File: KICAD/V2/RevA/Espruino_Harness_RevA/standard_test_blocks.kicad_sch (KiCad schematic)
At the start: 91 parts, among them J201 EXTERNAL_ANALOG_STIMULUS_0_TO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, J301 GROVE_I2C, J302 MCP23017_GPIO, J401 MCP3008_ANALOGUE_BREAKOUT, J402 PIHUT_MICROSD_BREAKOUT_106696, J501 DS18B20_SENSOR_A, J502 DS18B20_SENSOR_B, J503 2K2_DQ_4K7, J504 DS2413_MODULE, J701 UART_PEER_DIAGNOSTIC, J902 PIXEL_SHIFTER_6066, Q301 2N7002, Q302 2N7002, U301 MCP23017-E/SO, U401 MCP3008, U701 TMUX1511

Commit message: Implement RC01 routing baseline metadata
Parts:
- C301, C401, C402, C701, C901: AISLER_MPN (none) -> 100nF 10% 16V X7R 0603
- R308, R311, R705, R706, R707, R708: AISLER_MPN (none) -> 100k 0603 1% 0.1W
- TP101, TP102, TP103, TP104, TP201, TP202, TP203, TP204, TP205, TP301, TP302, TP303, TP304, TP305, TP306, TP401, TP402, TP501, TP502, TP503, TP504, TP505, TP901, TP902: MPN (none) -> 61300111121; now not fitted
- U701: MPN (none) -> TMUX1511PWR

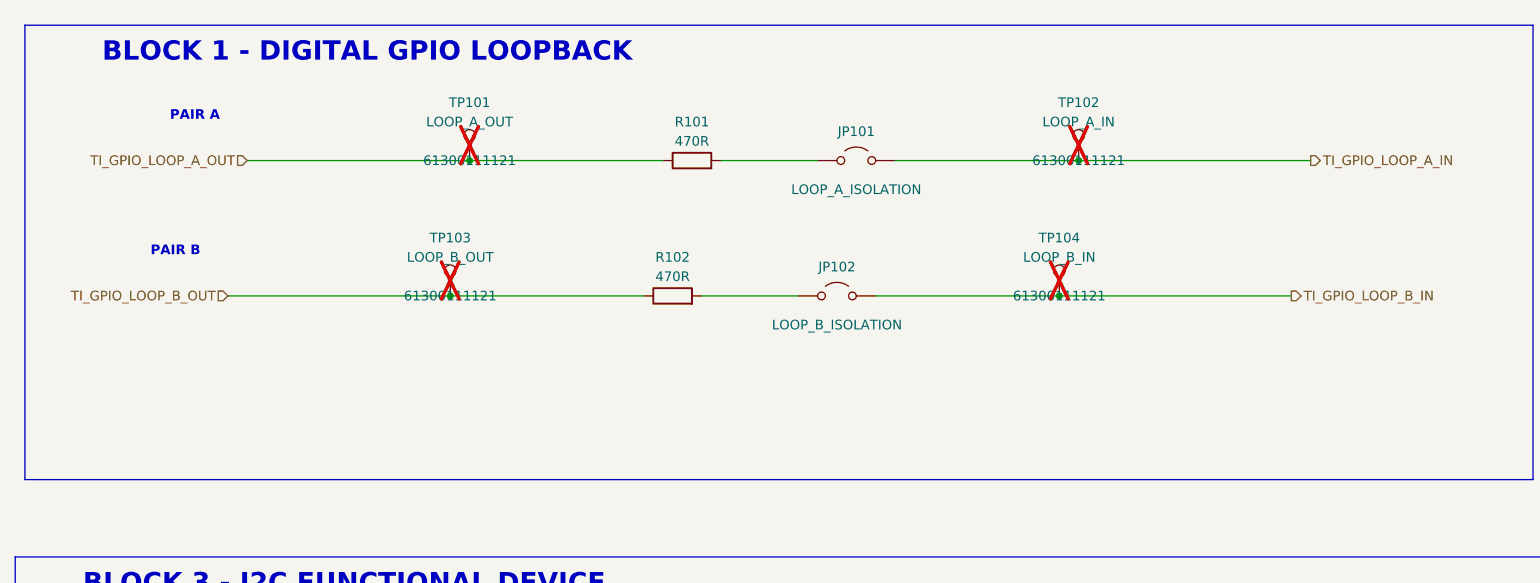
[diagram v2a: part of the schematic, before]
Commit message: Verify TB01 digital GPIO loopback baseline
Accept the two independent 470 ohm protected loopback paths using retained V1 functional evidence and Rev-A SMD component/package review.

Add the project-local isolation-header symbol, exact resistor/header/shunt metadata, focused visual evidence, deterministic TB01 contract, clean hierarchy ERC, synchronized PCB metadata and recorded downstream layout checks.
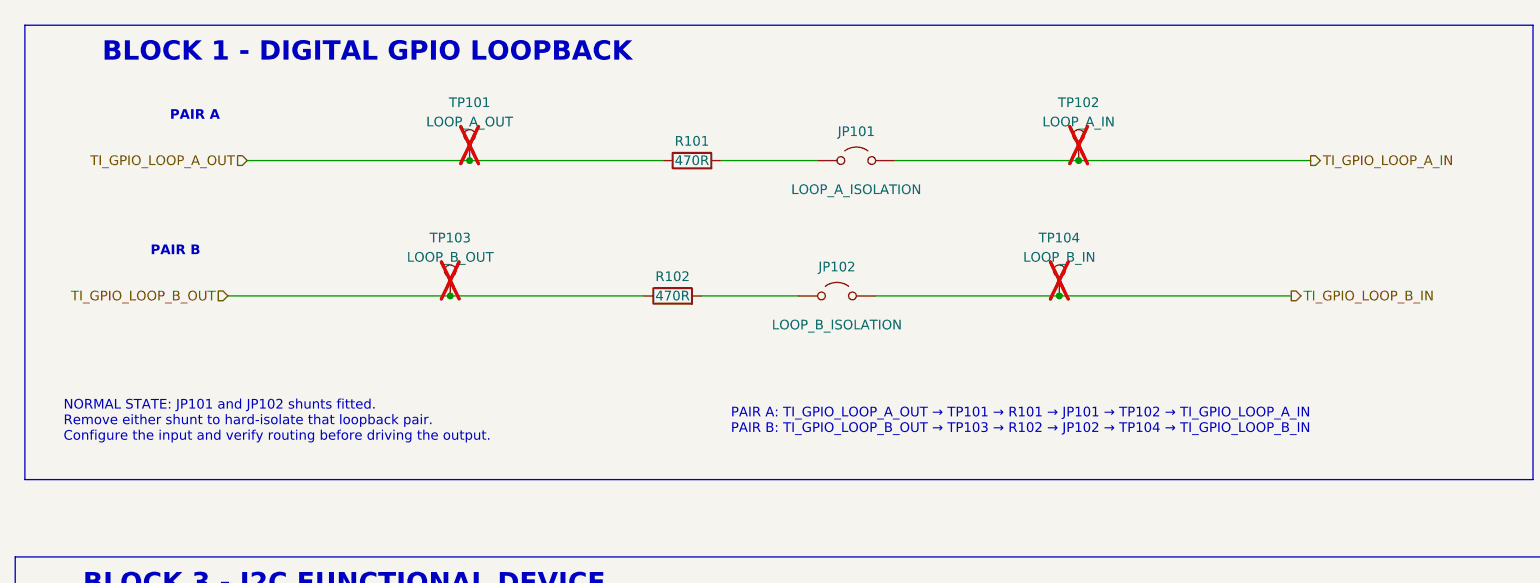
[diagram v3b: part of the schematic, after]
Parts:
- removed JP102: LOOP_B_ISOLATION, Connector_PinHeader_2.54mm:PinHeader_1x02_P2.54mm_Vertical, symbol Jumper:Jumper_2_Open
- added JP102: LOOP_B_ISOLATION, Connector_PinHeader_2.54mm:PinHeader_1x02_P2.54mm_Vertical, symbol Espruino_Harness_RevA:LOOPBACK_ISOLATION_HEADER
- JP101: symbol Jumper:Jumper_2_Open -> Espruino_Harness_RevA:LOOPBACK_ISOLATION_HEADER; MPN (none) -> 61300211121; SHUNT_MPN (none) -> 60900213421
- R101, R102: MPN (none) -> RC0603FR-07470RL
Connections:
- net TI_GPIO_LOOP_B_IN: now also JP102.2 (B)
- net at R102.2: now also JP102.1 (A)
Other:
- note added: "NORMAL STATE: JP101 and JP102 shunts fitted. Remove either shunt to hard-isolate that loopback pair. Configure the input and verify routing before driving the output."
- note added: "PAIR A: TI_GPIO_LOOP_A_OUT → TP101 → R101 → JP101 → TP102 → TI_GPIO_LOOP_A_IN PAIR B: TI_GPIO_LOOP_B_OUT → TP103 → R102 → JP102 → TP104 → TI_GPIO_LOOP_B_IN"
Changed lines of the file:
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@@
 		)
 	)
+	(text "NORMAL STATE: JP101 and JP102 shunts fitted.\nRemove either shunt to hard-isolate that loopback pair.\nConfigure the input and verify routing before driving the output."
+		(exclude_from_sim no)
+		(at 25.4 69.85 0)
+		(effects
+			(font
+				(size 1.27 1.27)
+			)
+			(justify left)
+		)
+	)
 	(text "Socketed DIP-16; CH0 = Block 2 ANALOG_FB"
 		(exclude_from_sim no)
@@
 		)
 	)
+	(text "PAIR A: TI_GPIO_LOOP_A_OUT → TP101 → R101 → JP101 → TP102 → TI_GPIO_LOOP_A_IN\nPAIR B: TI_GPIO_LOOP_B_OUT → TP103 → R102 → JP102 → TP104 → TI_GPIO_LOOP_B_IN"
+		(exclude_from_sim no)
+		(at 151.13 69.85 0)
+		(effects
+			(font
+				(size 1.27 1.27)
+			)
+		)
+	)
 	(text "External stimulus: 0 to 3.3 V; remove JP201"
 		(exclude_from_sim no)
@@
 		(dnp no)
 		(property "Reference" "R101"
-			(at 107.95 30.48 90)
+			(at 107.95 33.02 90)
 			(effects
 				(font
@@
 		)
 		(property "Value" "470R"
-			(at 107.95 33.02 90)
+			(at 107.95 35.56 90)
 			(effects
 				(font
@@
 			)
 		)
-		(property "Datasheet" "~"
+		(property "Datasheet" "https://www.yageogroup.com/component-documentation/download/specsheet/RC0603FR-07470RL"
+			(at 107.95 35.56 0)
+			(effects
+				(font
+					(size 1.27 1.27)
+				)
+				(hide yes)
+			)
+		)
+		(property "Description" "470 ohm, 1%, 0.1 W SMD loopback series-protection resistor"
 			(at 107.95 35.56 0)
 			(effects
@@
 			)
 		)
-		(property "Description" "470 ohm loopback series protection resistor; package not yet selected"
+		(property "MPN" "RC0603FR-07470RL"
 			(at 107.95 35.56 0)
 			(effects
@@
 			)
 		)
+		(property "AISLER_MPN" ""
+			(at 107.95 35.56 0)
+			(effects
+				(font
+					(size 1.27 1.27)
+				)
+			)
+		)
 		(pin "1"
 		)
@@
 					(size 1.27 1.27)
 				)
+				(hide yes)
 			)
 		)
@@
 	)
 	(symbol
-		(lib_id "Jumper:Jumper_2_Open")
+		(lib_id "Espruino_Harness_RevA:LOOPBACK_ISOLATION_HEADER")
 		(at 129.54 35.56 0)
 		(unit 1)
@@
 			)
 		)
-		(property "Datasheet" "~"
+		(property "Datasheet" "https://www.we-online.com/components/products/datasheet/61300211121.pdf"
+			(at 129.54 35.56 0)
+			(effects
+				(font
+					(size 1.27 1.27)
+				)
+				(hide yes)
+			)
+		)
+		(property "Description" "2.54 mm two-pin THT loopback isolation header; shunt 60900213421 fitted for normal operation"
 			(at 129.54 35.56 0)
 			(effects
@@
 			)
 		)
-		(property "Description" "2.54 mm two-pin isolation header; shunt fitted for normal operation"
+		(property "MPN" "61300211121"
+			(at 129.54 35.56 0)
+			(effects
+				(font
+					(size 1.27 1.27)
+				)
+				(hide yes)
+			)
+		)
+		(property "AISLER_MPN" ""
+			(at 129.54 35.56 0)
+			(effects
+				(font
+					(size 1.27 1.27)
+				)
+			)
+		)
+		(property "SHUNT_MPN" "60900213421"
 			(at 129.54 35.56 0)
 			(effects
@@
 	)
 	(symbol
+		(lib_id "Espruino_Harness_RevA:LOOPBACK_ISOLATION_HEADER")
+		(at 127 53.34 0)
+		(unit 1)
+		(exclude_from_sim no)
+		(in_bom yes)
+		(on_board yes)
+		(dnp no)
+		(property "Reference" "JP102"
+			(at 127 49.53 0)
+			(effects
+				(font
+					(size 1.27 1.27)
+				)
+			)
+		)
+		(property "Value" "LOOP_B_ISOLATION"
+			(at 127 57.15 0)
+			(effects
+				(font
+					(size 1.27 1.27)
+				)
+			)
+		)
+		(property "Footprint" "Connector_PinHeader_2.54mm:PinHeader_1x02_P2.54mm_Vertical"
+			(at 127 53.34 0)
+			(effects
+				(font
+					(size 1.27 1.27)
+				)
+				(hide yes)
+			)
+		)
+		(property "Datasheet" "https://www.we-online.com/components/products/datasheet/61300211121.pdf"
+			(at 127 53.34 0)
+			(effects
+				(font
+					(size 1.27 1.27)
+				)
+				(hide yes)
+			)
+		)
+		(property "Description" "2.54 mm two-pin THT loopback isolation header; shunt 60900213421 fitted for normal operation"
+			(at 127 53.34 0)
+			(effects
+				(font
+					(size 1.27 1.27)
+				)
+				(hide yes)
+			)
+		)
+		(property "MPN" "61300211121"
+			(at 127 53.34 0)
+			(effects
+				(font
+					(size 1.27 1.27)
+				)
+				(hide yes)
+			)
+		)
+		(property "AISLER_MPN" ""
+			(at 127 53.34 0)
+			(effects
+				(font
+					(size 1.27 1.27)
+				)
+			)
+		)
+		(property "SHUNT_MPN" "60900213421"
+			(at 127 53.34 0)
+			(effects
+				(font
+					(size 1.27 1.27)
+				)
+				(hide yes)
+			)
+		)
+		(pin "1"
+		)
+		(pin "2"
+		)
+		(instances
+			(project "Espruino_Harness_RevA"
+				(path "/12444148-a051-4fb0-ae7b-e3d34eecc954/de8f4588-cd43-45f8-a502-51219f80935f"
+					(reference "JP102")
+					(unit 1)
+				)
+			)
+		)
+	)
+	(symbol
 		(lib_id "Device:C")
 		(at 134.62 127 90)
@@
 					(size 1.27 1.27)
 				)
+				(hide yes)
 			)
 		)
@@
 	)
 	(symbol
-		(lib_id "Device:R")
-		(at 105.41 53.34 90)
-		(unit 1)
-		(exclude_from_sim no)
-		(in_bom yes)
-		(on_board yes)
-		(dnp no)
-		(property "Reference" "R102"
-			(at 105.41 48.26 90)
-			(effects
-				(font
-					(size 1.27 1.27)
-				)
-			)
-		)
-		(property "Value" "470R"
-			(at 105.41 50.8 90)
-			(effects
-				(font
-					(size 1.27 1.27)
-				)
-			)
-		)
-		(property "Footprint" "Resistor_SMD:R_0603_1608Metric"
-			(at 105.41 55.118 90)
-			(effects
-				(font
-					(size 1.27 1.27)
-				)
-				(hide yes)
-			)
-		)
-		(property "Datasheet" "~"
-			(at 105.41 53.34 0)
-			(effects
-				(font
-					(size 1.27 1.27)
-				)
-				(hide yes)
-			)
-		)
-		(property "Description" "470 ohm loopback series protection resistor; package not yet selected"
-			(at 105.41 53.34 0)
-			(effects
-				(font
-					(size 1.27 1.27)
-				)
-				(hide yes)
-			)
-		)
-		(pin "1"
-		)
-		(pin "2"
-		)
-		(instances
-			(project "Espruino_Harness_RevA"
-				(path "/12444148-a051-4fb0-ae7b-e3d34eecc954/de8f4588-cd43-45f8-a502-51219f80935f"
-					(reference "R102")
-					(unit 1)
-				)
-			)
-		)
-	)
-	(symbol
 		(lib_id "Jumper:Jumper_2_Open")
 		(at 121.92 115.57 90)
@@
 	)
 	(symbol
-		(lib_id "Jumper:Jumper_2_Open")
-		(at 127 53.34 0)
-		(unit 1)
-		(exclude_from_sim no)
-		(in_bom yes)
-		(on_board yes)
-		(dnp no)
-		(property "Reference" "JP102"
-			(at 127 49.53 0)
-			(effects
-				(font
-					(size 1.27 1.27)
-				)
-			)
-		)
-		(property "Value" "LOOP_B_ISOLATION"
-			(at 127 57.15 0)
-			(effects
-				(font
-					(size 1.27 1.27)
-				)
-			)
-		)
-		(property "Footprint" "Connector_PinHeader_2.54mm:PinHeader_1x02_P2.54mm_Vertical"
-			(at 127 53.34 0)
-			(effects
-				(font
-					(size 1.27 1.27)
-				)
-				(hide yes)
-			)
-		)
-		(property "Datasheet" "~"
-			(at 127 53.34 0)
-			(effects
-				(font
-					(size 1.27 1.27)
-				)
-				(hide yes)
-			)
-		)
-		(property "Description" "2.54 mm two-pin isolation header; shunt fitted for normal operation"
-			(at 127 53.34 0)
-			(effects
-				(font
-					(size 1.27 1.27)
-				)
-				(hide yes)
-			)
-		)
-		(pin "1"
-		)
-		(pin "2"
-		)
-		(instances
-			(project "Espruino_Harness_RevA"
-				(path "/12444148-a051-4fb0-ae7b-e3d34eecc954/de8f4588-cd43-45f8-a502-51219f80935f"
-					(reference "JP102")
-					(unit 1)
-				)
-			)
-		)
-	)
-	(symbol
 		(lib_id "Espruino_Harness_RevA:TMUX1511_PW")
 		(at 107.95 254 0)
@@
 					(size 1.27 1.27)
 				)
+				(hide yes)
 			)
 		)
@@
 	)
 	(symbol
+		(lib_id "Device:R")
+		(at 105.41 53.34 90)
+		(unit 1)
+		(exclude_from_sim no)
+		(in_bom yes)
+		(on_board yes)
+		(dnp no)
+		(property "Reference" "R102"
+			(at 105.41 50.8 90)
+			(effects
+				(font
+					(size 1.27 1.27)
+				)
+			)
+		)
+		(property "Value" "470R"
+			(at 105.41 53.34 90)
+			(effects
+				(font
+					(size 1.27 1.27)
+				)
+			)
+		)
+		(property "Footprint" "Resistor_SMD:R_0603_1608Metric"
+			(at 105.41 55.118 90)
+			(effects
+				(font
+					(size 1.27 1.27)
+				)
+				(hide yes)
+			)
+		)
+		(property "Datasheet" "https://www.yageogroup.com/component-documentation/download/specsheet/RC0603FR-07470RL"
+			(at 105.41 53.34 0)
+			(effects
+				(font
+					(size 1.27 1.27)
+				)
+				(hide yes)
+			)
+		)
+		(property "Description" "470 ohm, 1%, 0.1 W SMD loopback series-protection resistor"
+			(at 105.41 53.34 0)
+			(effects
+				(font
+					(size 1.27 1.27)
+				)
+				(hide yes)
+			)
+		)
+		(property "MPN" "RC0603FR-07470RL"
+			(at 105.41 53.34 0)
+			(effects
+				(font
+					(size 1.27 1.27)
+				)
+				(hide yes)
+			)
+		)
+		(property "AISLER_MPN" ""
+			(at 105.41 53.34 0)
+			(effects
+				(font
+					(size 1.27 1.27)
+				)
+			)
+		)
+		(pin "1"
+		)
+		(pin "2"
+		)
+		(instances
+			(project "Espruino_Harness_RevA"
+				(path "/12444148-a051-4fb0-ae7b-e3d34eecc954/de8f4588-cd43-45f8-a502-51219f80935f"
+					(reference "R102")
+					(unit 1)
+				)
+			)
+		)
+	)
+	(symbol
 		(lib_id "Jumper:Jumper_2_Open")
 		(at 485.14 25.4 0)
@@
 					(size 1.27 1.27)
 				)
+				(hide yes)
 			)
 		)
